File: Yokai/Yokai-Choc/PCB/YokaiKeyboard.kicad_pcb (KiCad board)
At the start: 2 copper layers, 161.8 x 114.7 mm, 135 parts, among them J2 4PIN, J3 OLED, P1 i2c_pin, P2 i2c_pin, SW1 SW_PUSH-MX_W_LED, SW10 SW_PUSH-MX_W_LED, SW11 SW_PUSH-MX_W_LED, SW12 SW_PUSH-MX_W_LED, SW13 SW_PUSH-MX_W_LED, SW14 SW_PUSH-MX_W_LED, SW15 SW_PUSH-MX_W_LED, SW16 SW_PUSH-MX_W_LED, SW17 SW_PUSH-MX_W_LED, SW18 SW_PUSH-MX_W_LED, SW19 SW_PUSH-MX_W_LED, SW2 SW_PUSH-MX_W_LED, SW20 SW_PUSH-MX_W_LED, SW21 SW_PUSH-MX_W_LED, SW22 SW_PUSH-MX_W_LED, SW23 SW_PUSH-MX_W_LED, SW24 SW_PUSH-MX_W_LED, SW25 SW_PUSH-MX_W_LED, SW26 SW_PUSH-MX_W_LED, SW27 SW_PUSH-MX_W_LED, SW28 SW_PUSH-MX_W_LED, SW29 SW_PUSH-MX_W_LED, SW3 SW_PUSH-MX_W_LED, SW30 SW_PUSH-MX_W_LED, SW31 SW_PUSH-MX_W_LED, SW32 SW_PUSH-MX_W_LED, SW33 SW_PUSH-MX_W_LED, SW34 SW_PUSH-MX_W_LED, SW35 SW_PUSH-MX_W_LED, SW36 Rotary_Encoder, SW37 SW_PUSH-MX_W_LED, SW4 SW_PUSH-MX_W_LED, SW5 SW_PUSH-MX_W_LED, SW6 SW_PUSH-MX_W_LED, SW7 SW_PUSH-MX_W_LED, SW8 SW_PUSH-MX_W_LED, SW9 SW_PUSH-MX_W_LED, U1 nice_nano

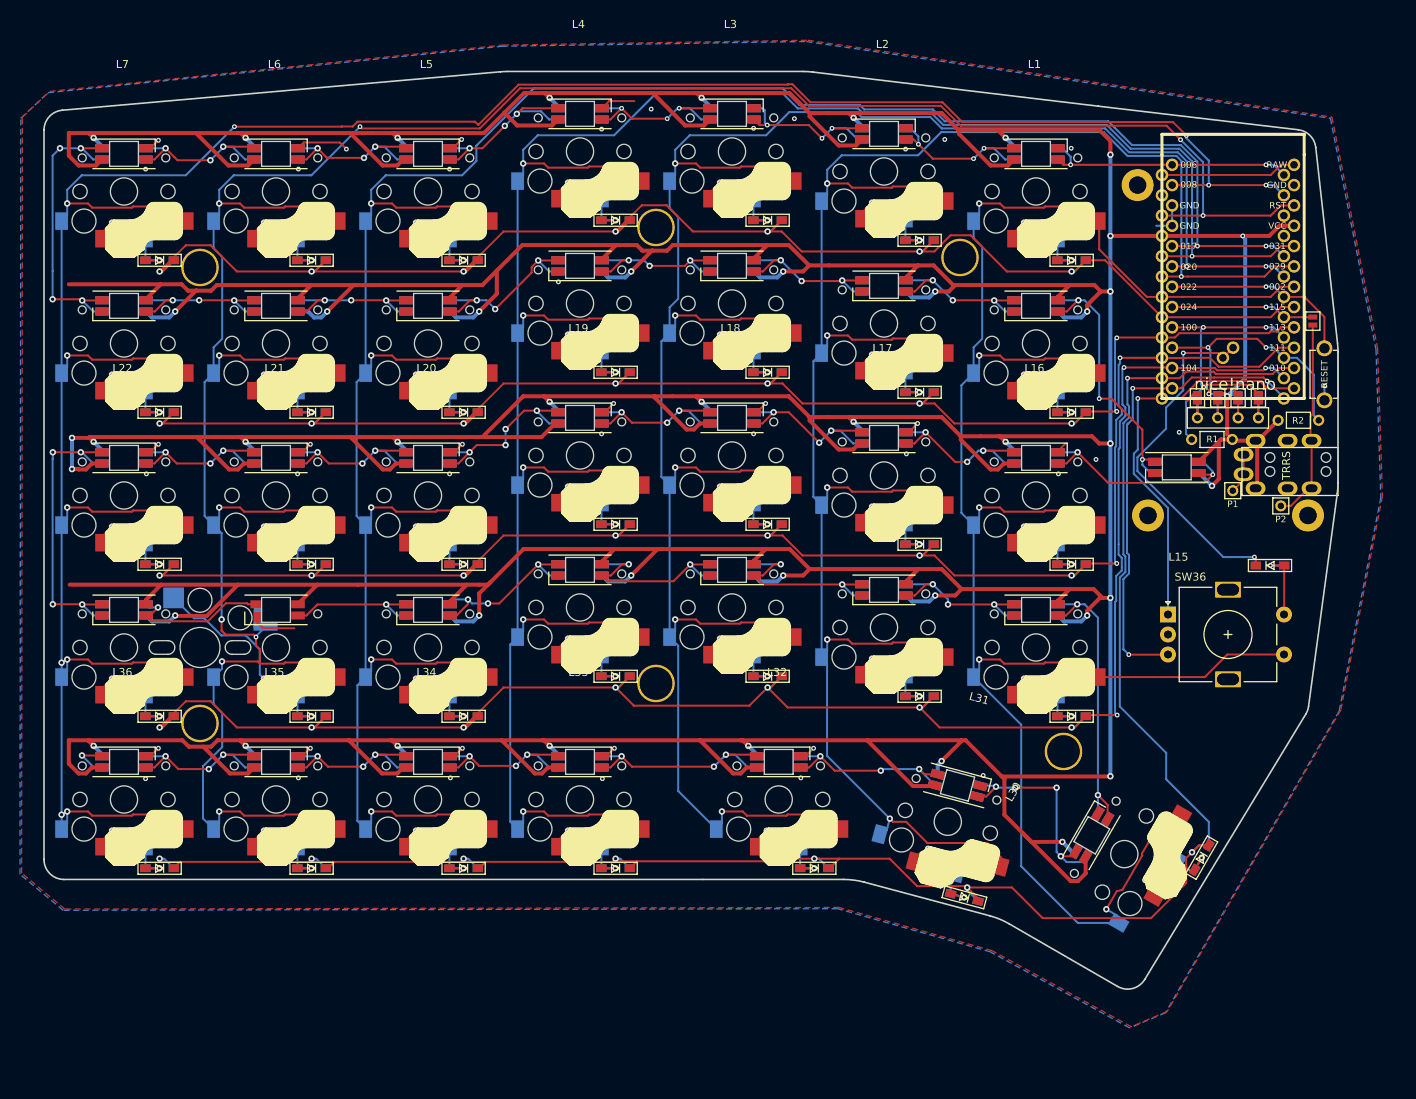
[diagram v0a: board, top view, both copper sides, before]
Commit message: Add files via upload
*Increased pinky stagger
*Inverted stabilizer cutouts
*Added additional thumb key
*Minor footprint changes
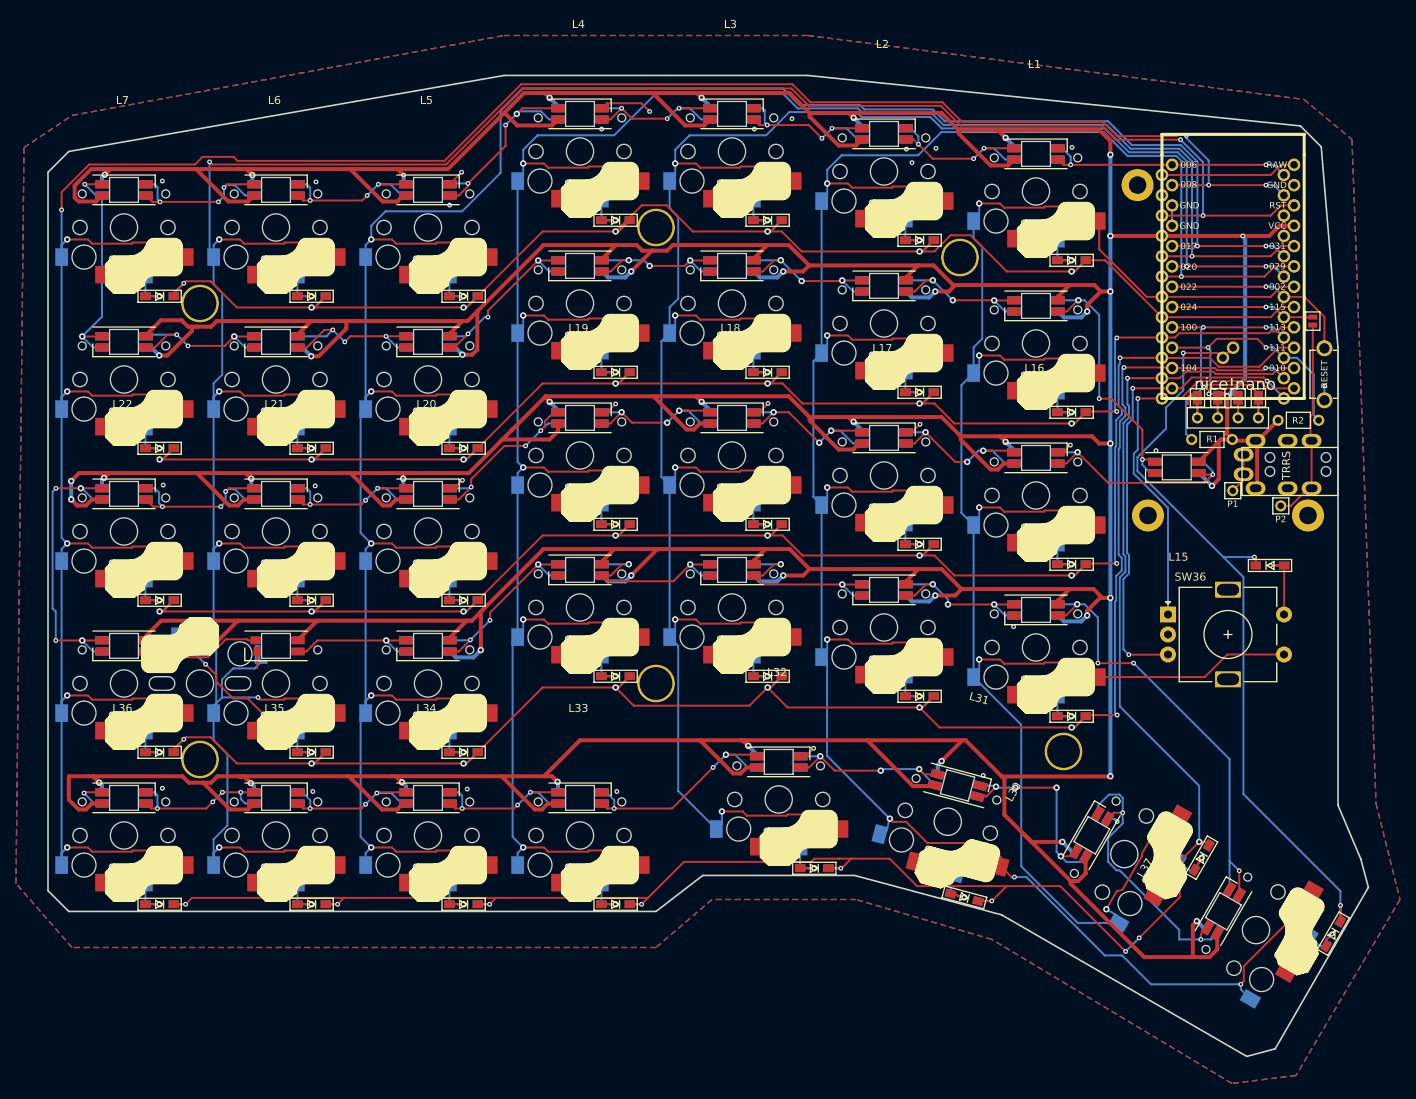
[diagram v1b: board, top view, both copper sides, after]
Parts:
- added D37: D, Yokai:smd_diode, F.Cu at (220.7, 142.3)
- added L37: LED_sk2812_SM, Yokai:YS-SK6812MINI-E-DoubleSide, F.Cu at (206.9, 139.5)
- added SW38: SW_PUSH-MX_W_LED, Yokai:Choc_Hotswap_DoubleSide, F.Cu at (211.0, 141.8)
- D1, D10, D11, D12, D13, D14, D15, D16, D17, D18, D19, D2, D20, D21, D22, D23, D24, D25, D26, D27, D28, D29, D3, D30, D31, D32, D33, D34, D35, D36, D4, D5, D6, D7, D8, D9: footprint SofleRGB:crkbd-diode -> Yokai:smd_diode
- J2: footprint SofleRGB:MJ-4PP-9 -> Yokai:MJ-4PP-9
- J3: footprint SofleRGB:OLED_4Pin -> Yokai:OLED_4Pin
- JP1, JP2, JP3, JP4, JP5, JP6, JP7, JP8, W1: footprint SofleRGB:Jumper -> Yokai:Jumper
- L1, L10, L11, L12, L13, L14, L15, L16, L17, L18, L19, L2, L20, L21, L22, L23, L24, L25, L26, L27, L28, L29, L3, L30, L31, L32, L33, L34, L35, L36, L4, L5, L6, L7, L8, L9: footprint Keebio-Parts:YS-SK6812MINI-E-DoubleSide -> Yokai:YS-SK6812MINI-E-DoubleSide
- P1, P2: footprint SofleRGB:1pin_conn -> Yokai:1pin_conn
- R1, R2: footprint SofleRGB:RESISTOR_mini -> Yokai:RESISTOR_mini
- RSW1: footprint SofleRGB:TACT_SWITCH_TVBP06 -> Yokai:TACT_SWITCH_TVBP06
- SW1, SW10, SW11, SW12, SW13, SW14, SW15, SW16, SW17, SW18, SW19, SW2, SW20, SW21, SW22, SW23, SW24, SW25, SW26, SW27, SW28, SW29, SW3, SW30, SW31, SW32, SW33, SW34, SW35, SW4, SW5, SW6, SW7, SW8, SW9: footprint kbd:Choc_Hotswap_DoubleSide -> Yokai:Choc_Hotswap_DoubleSide
- SW37: footprint kbd:ChocV1_V2_Hotswap -> Yokai:Choc_Hotswap_DoubleSide
- TH1, TH2, TH9: footprint SofleRGB:M2_HOLE_PCB -> Yokai:M2_HOLE_PCB
- TH3, TH4, TH5, TH6, TH7, TH8: footprint SofleRGB:HOLE_M2_TH -> Yokai:HOLE_M2_TH
- U1: footprint Keebio-Parts:nice_nano -> Yokai:nice_nano
- moved D12 4.50 mm to (112.0, 81.6)
- moved D13 4.50 mm to (93.0, 81.6)
- moved D14 4.50 mm to (74.0, 81.6)
- moved D19 4.50 mm to (112.0, 100.6)
- moved D20 4.50 mm to (93.0, 100.6)
- moved D21 4.50 mm to (74.0, 100.6)
- moved D26 4.50 mm to (112.0, 119.6)
- moved D27 4.50 mm to (93.0, 119.6)
- moved D28 4.50 mm to (74.0, 119.6)
- moved D32 4.50 mm to (130.9, 138.6)
- moved D33 4.50 mm to (112.0, 138.6)
- moved D34 4.50 mm to (93.0, 138.6)
- moved D35 4.50 mm to (74.0, 138.6)
- moved D5 4.50 mm to (112.0, 62.6)
- moved D6 4.50 mm to (93.0, 62.6)
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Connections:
- L30 pad 4: Net-(L23-Pad2) -> Net-(L30-Pad4)
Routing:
- net col1: track 256.2 -> 311.0 mm, vias 6 -> 8
- net row5: track 45.5 -> 99.0 mm, vias 2 -> 3
- net Net-(L30-Pad4): track 0.00 -> 36.3 mm, vias 0 -> 2
- net Net-(L23-Pad2): track 36.6 -> 56.8 mm, vias 2 -> 4
- net GND: track 51.6 -> 37.3 mm, vias 41 -> 29
- net Net-(D37-Pad2): track 0.00 -> 14.3 mm, vias 0 -> 2
- net VCC: track 1248.1 -> 1261.4 mm, vias 45 -> 46
- net 2uCol: track 338.1 -> 348.0 mm, vias 10 -> 8
- net Net-(L14-Pad4): track 37.0 -> 29.4 mm, vias 4 -> 2
- net col6: track 340.6 -> 346.1 mm, vias 11 -> 9
- net row3: track 225.2 -> 220.0 mm
- net row0: track 187.7 -> 182.5 mm
- net row4: track 251.7 -> 256.0 mm, vias 8 -> 10
- net Net-(L4-Pad2): track 24.3 -> 27.7 mm
- net Net-(L12-Pad4): track 20.4 -> 23.1 mm
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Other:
- board size 161.8 x 114.7 mm -> 165.1 x 122.6 mm
